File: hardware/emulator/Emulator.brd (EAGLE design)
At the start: 65.5 x 72.1 mm, 28 parts, among them U1 PDM1-S5-D12-S, U2 LM6132BIN, U3 OPA2277PA, U4 L7908CV, U5 L7808ABV, U6 TEENSY_3.6_DIL, U7 ZVP2106ASTZ

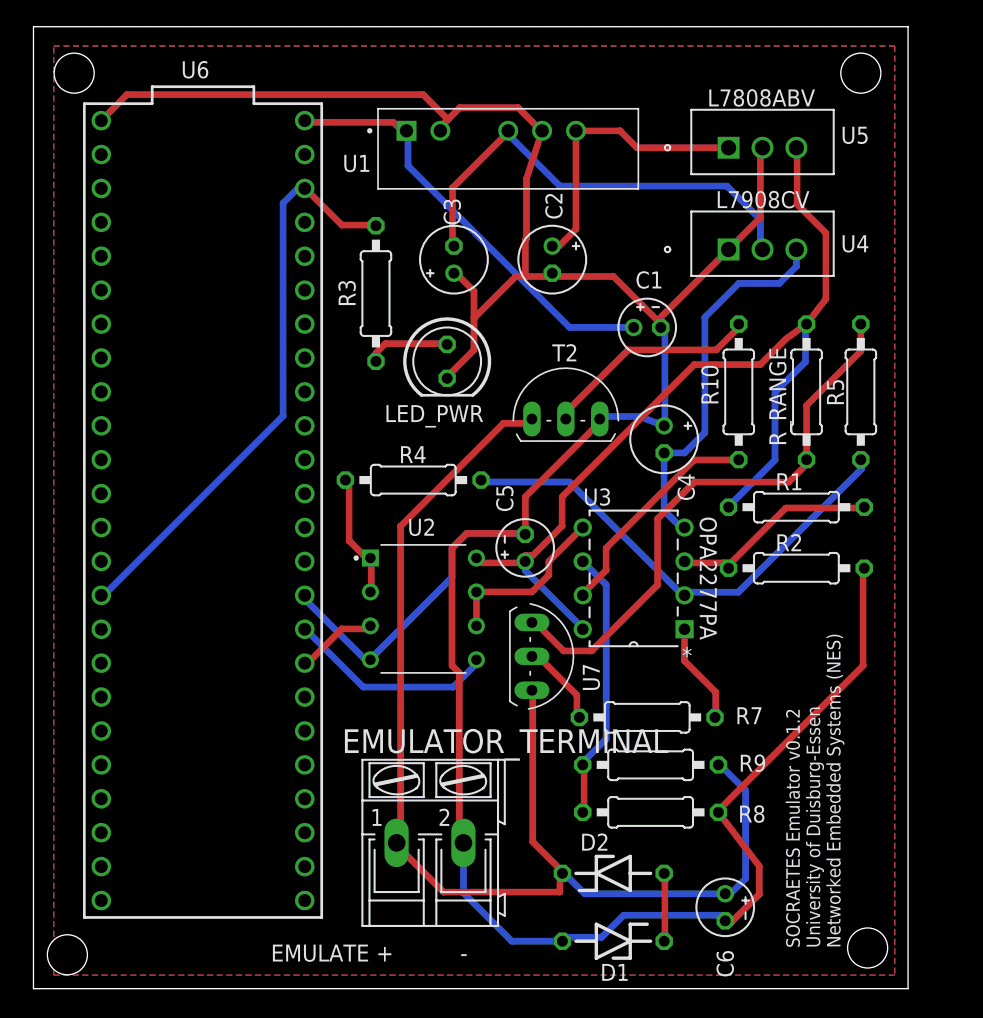
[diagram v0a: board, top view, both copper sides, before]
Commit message: Add a capacitor to the solar cell model op amp for stability of the op amp's output
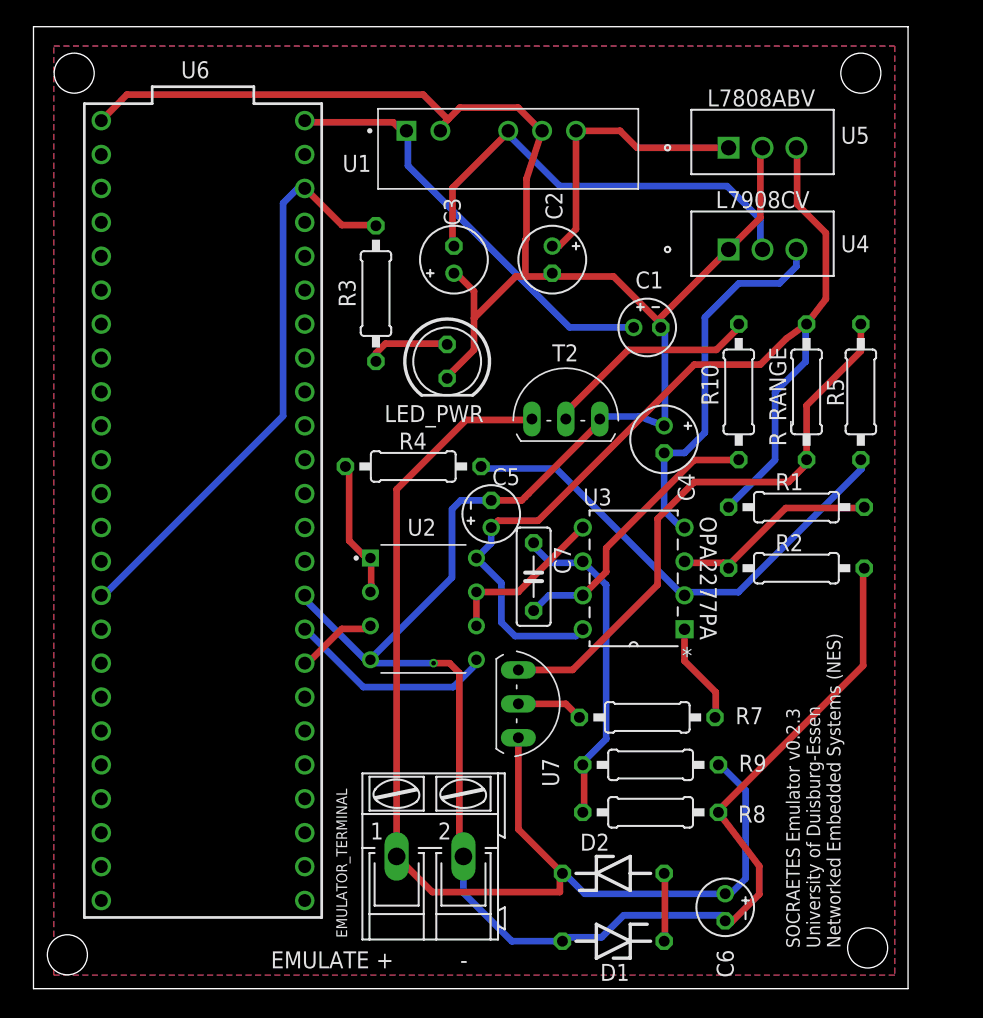
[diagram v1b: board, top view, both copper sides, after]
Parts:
- added C7: 10pF, rcl:C050-025X075
- T2: value (none) -> 2N5401
- moved U7 3.70 mm to (36.3, 21.3)
- moved C5 3.59 mm to (34.3, 35.6)
- moved EMULATOR_TERMINAL 1.02 mm to (29.7, 9.91)
- moved R4 1.02 mm to (28.4, 39.1)
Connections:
- net N$11: now also C7.1
- net N$13: now also C7.2
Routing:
- net GND: track 225.9 -> 217.5 mm, vias 0 -> 1
- net N$11: track 20.3 -> 24.9 mm
- net +8V: track 71.3 -> 75.6 mm
- net N$13: track 16.9 -> 21.1 mm
- net N$5: track 6.93 -> 4.99 mm
- net DAC_SC_CURRENT_EMULATION_BUFFERED: track 9.35 -> 10.4 mm
- net N$7: track 42.3 -> 43.0 mm
- net DAC_OC_VOLTAGE_EMULATION_BUFFERED: track 13.1 -> 12.5 mm
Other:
- board text added: "SOCRAETES Emulator v0.2.3 University of Duisburg-Essen Networked Embedded Systems (NES)"
- board text removed: "SOCRAETES Emulator v0.1.2 University of Duisburg-Essen Networked Embedded Systems (NES)"

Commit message: Migrate emulator board to Teensy 4.1
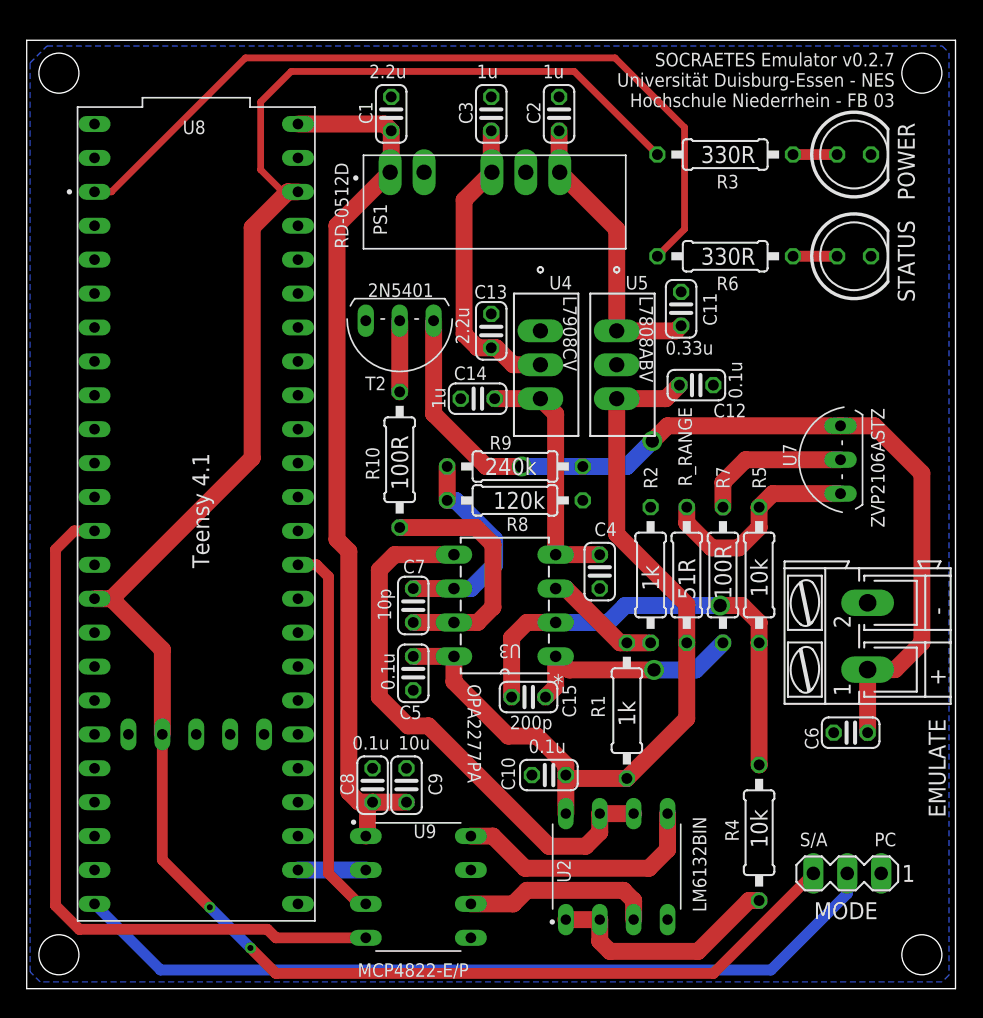
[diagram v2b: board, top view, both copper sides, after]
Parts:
- removed D1, D2: 3v3, diode:ZDIO-7.5
- removed LED_PWR: (no value), led:LED5MM
- removed U1: PDM1-S5-D12-S, PDM1-S5-D12-S:CONV_PDM1-S5-D12-S
- removed U6: TEENSY_3.6_DIL, Teensy_3_and_LC_Series_Boards_v1.4:TEENSY_3.6_DIL
- added C10, C12, C8: 0.1u, rcl:C025-024X044
- added C11: 0.33u, rcl:C025-024X044
- added C13: 2.2u, rcl:C025-024X044
- added C14: 1u, rcl:C025-024X044
- added C15: 200p, rcl:C025-024X044
- added C9: 10u, rcl:C025-024X044
- added MODE: (no value), con-lstb:MA03-1
- added POWER, STATUS: (no value), led:LED5MM
- added PS1: RD-0512D, RD-0512D:CONV_RD-0512D
- added R6: 330R, rcl:0207/10
- added U8: DEV-16771_REDUCED_PINS, DEV-16771 (Teensy 41):MODULE_DEV-16771_REDUCED_PINS
- added U9: MCP4822-E/P, MCP4822-E_P:DIP787W46P254L927H533Q8
- C1, C5, C6: device rcl:E2-4 -> rcl:C025-024X044
- C2, C3: device rcl:E2-5 -> rcl:C025-024X044
- C4: value 1u -> 0.1u; device rcl:E2-5 -> rcl:C025-024X044
- C7: value 10pF -> 10p; device rcl:C050-025X075 -> rcl:C025-024X044
- R_RANGE: value 51 -> 51R
- moved R4 37.7 mm to (54.4, 11.7), turned to 270 degrees
- moved EMULATOR_TERMINAL 36.7 mm to (62.5, 26.4), turned to 90 degrees
- moved U7 30.3 mm to (60.5, 39.6), turned to 90 degrees
- moved R3 28.2 mm to (51.8, 62.5), turned to 180 degrees
- moved R10 25.9 mm to (27.4, 39.6)
- moved R8 25.5 mm to (36.1, 36.6)
- moved C1 25.0 mm to (26.8, 65.5), turned to 90 degrees
- moved R9 24.6 mm to (36.1, 39.1)
- moved U2 24.1 mm to (43.7, 9.14), turned to 90 degrees
- moved R1 19.8 mm to (44.5, 20.8), turned to 270 degrees
- moved R_RANGE 16.4 mm to (48.9, 31.0), turned to 270 degrees
- moved C6 16.1 mm to (61.2, 19.2), turned to 0 degrees
- moved U5 16.1 mm to (43.7, 49.3), turned to 270 degrees
- moved R5 15.7 mm to (54.4, 31.0)
- moved U4 15.4 mm to (38.0, 49.3), turned to 270 degrees
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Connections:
- removed net AGND: U6.AGND
- removed net N$4: D1.C, D2.A
- removed net N$8: R4.1, R5.2, U3.2
- new net +5V: C1.1, C8.1, C9.1, PS1.1, U8.VIN, U9.1
- new net DAC_CS: U8.34, U9.2
- new net DAC_MOSI: U8.11, U9.4
- new net DAC_SCK: U8.13, U9.3
- new net JUMPER_SELECT_MODE: MODE.2, U8.32
- new net N$3: C15.1, R4.1, R5.2, U3.2
- new net STATUS_LED: R6.2, U8.1
- net +12V: now also C11.1, C2.1, PS1.6; no longer C2.+, U1.6
- net +3V3: now also MODE.3, U8.3.3V_1, U8.3.3V_2, U8.3.3V_3; no longer U6.3.3V, U6.3.3V3
- net +8V: now also C10.2, C12.2, C5.2; no longer C5.+
- net -12V: now also C13.2, C3.1, PS1.4; no longer C3.-, U1.4
- net -8V: now also C14.2, C4.2; no longer C4.-
- net DAC_OC_VOLTAGE_EMULATION: now also U9.8; no longer U6.A22
- net DAC_SC_CURRENT_EMULATION: now also U9.6; no longer U6.A21
- net GND: now also C1.2, C10.1, C11.2, C12.1, C13.1, C14.1, C2.2, C3.2, C4.1, C5.1, C6.1, C8.2, C9.2, MODE.1, POWER.K, PS1.2, PS1.5, STATUS.K, U8.GND1, U8.GND2, U8.GND3, U8.GND4, U9.5, U9.7; no longer C1.-, C2.-, C3.+, C4.+, C5.-, C6.-, D1.A, LED_PWR.K, U1.2, U1.5, U6.GND, U6.GND1
- net HARVESTER_EMULATION: now also C6.2; no longer C6.+, D2.C
- net N$2: now also R6.1, STATUS.A; no longer C1.+, U1.1, U6.VIN
- net N$6: now also C15.2
- net N$9: now also POWER.A; no longer LED_PWR.A
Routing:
- net GND: track 217.5 -> 0.00 mm, vias 1 -> 0
- net +3V3: track 43.7 -> 156.3 mm, vias 0 -> 2
- net +5V: track 0.00 -> 66.2 mm
- net JUMPER_SELECT_MODE: track 0.00 -> 62.3 mm
- net STATUS_LED: track 0.00 -> 61.0 mm
- net DAC_MOSI: track 0.00 -> 54.4 mm
- net N$8: track 37.2 -> 0.00 mm
- net N$3: track 0.00 -> 35.2 mm, vias 0 -> 1
- net N$2: track 32.5 -> 3.30 mm
- net DAC_SCK: track 0.00 -> 28.6 mm
- net DAC_OC_VOLTAGE_EMULATION_BUFFERED: track 12.5 -> 41.1 mm
- net N$7: track 43.0 -> 16.0 mm
- net HARVESTER_EMULATION: track 91.0 -> 70.2 mm, vias 0 -> 2
- net +8V: track 75.6 -> 61.8 mm
- net -12V: track 34.5 -> 22.8 mm
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- removed copper zone on layer 1, net GND
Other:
- board size 65.5 x 72.1 mm -> 69.6 x 71 mm
- board text added: "PC"
- board text added: "S/A"
- board text added: "SOCRAETES Emulator v0.2.7 Universität Duisburg-Essen - NES Hochschule Niederrhein - FB 03"
- board text removed: "SOCRAETES Emulator v0.2.3 University of Duisburg-Essen Networked Embedded Systems (NES)"

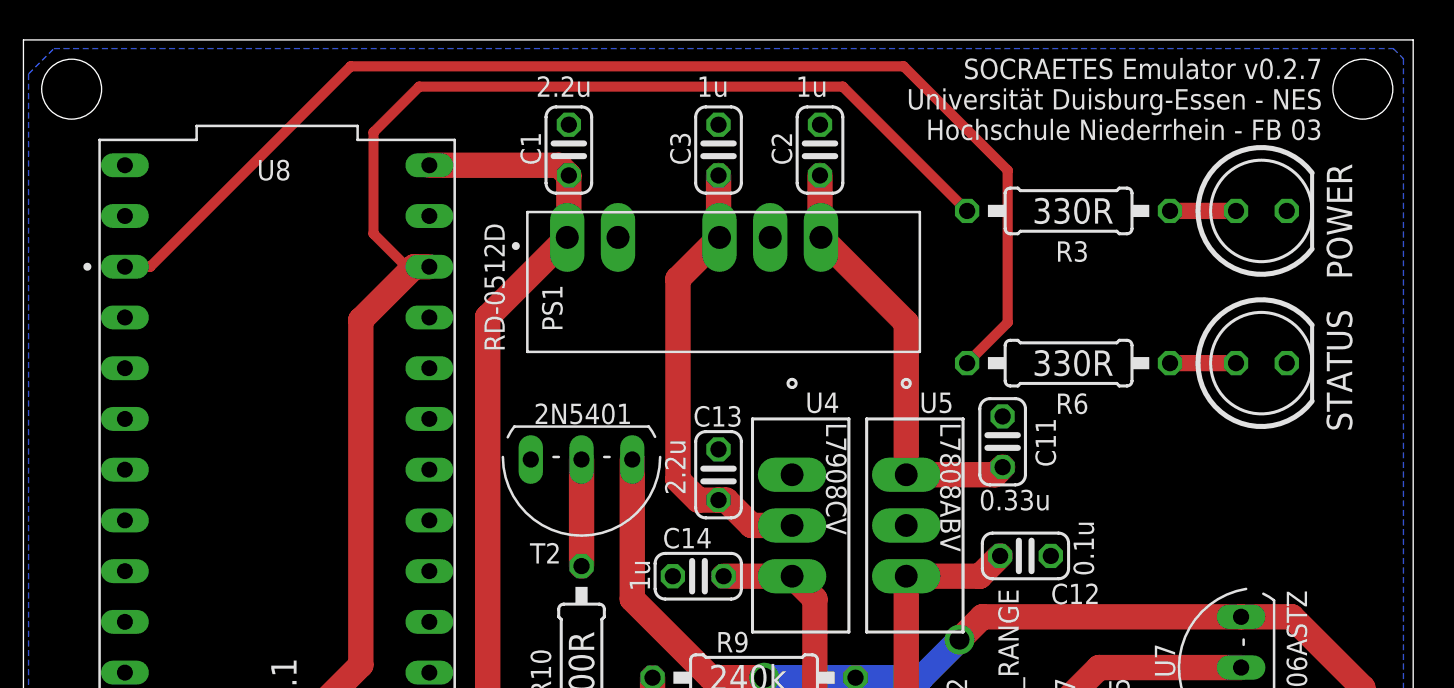
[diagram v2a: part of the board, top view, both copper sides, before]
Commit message: Add error LED to the board
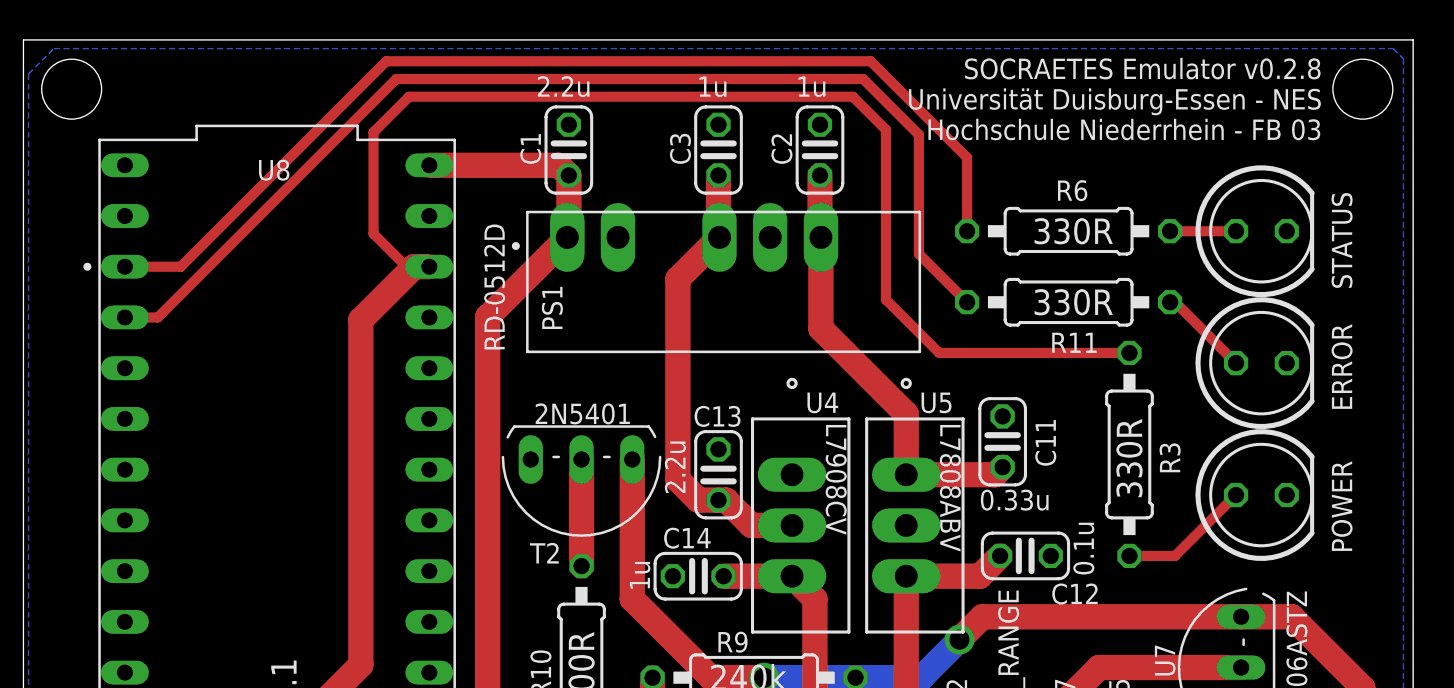
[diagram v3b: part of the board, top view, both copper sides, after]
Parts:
- added ERROR: (no value), led:LED5MM
- added R11: 330R, rcl:0207/10
- moved POWER 14.2 mm to (61.5, 48.3)
- moved R3 12.6 mm to (54.9, 50.3), turned to 90 degrees
- moved R6 6.60 mm to (51.8, 61.5)
- moved STATUS 6.60 mm to (61.5, 61.5)
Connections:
- new net ERROR_LED: R11.2, U8.2
- new net N$4: ERROR.A, R11.1
- net GND: now also ERROR.K
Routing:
- net ERROR_LED: track 0.00 -> 55.2 mm
- net +3V3: track 156.3 -> 172.0 mm
- net STATUS_LED: track 61.0 -> 52.1 mm
- net N$4: track 0.00 -> 4.56 mm
- net N$9: track 3.30 -> 6.60 mm
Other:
- board text added: "SOCRAETES Emulator v0.2.8 Universität Duisburg-Essen - NES Hochschule Niederrhein - FB 03"
- board text removed: "SOCRAETES Emulator v0.2.7 Universität Duisburg-Essen - NES Hochschule Niederrhein - FB 03"
